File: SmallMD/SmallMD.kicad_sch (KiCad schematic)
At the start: 162 parts

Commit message: 回路設計
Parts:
- removed R? (x2): 1k, Resistor_SMD:R_0402_1005Metric, symbol Device:R
- removed R? (x2): 510, Resistor_SMD:R_0402_1005Metric, symbol Device:R
- removed U? (x2): TLP785, Package_DIP:DIP-4_W7.62mm, symbol Isolator:TLP785
- added C? (x4): 0.1uF, Capacitor_SMD:C_0402_1005Metric, symbol Device:C
- added JP? (x3): Jumper_2_Open, Connector_PinHeader_2.54mm:PinHeader_1x02_P2.54mm_Vertical, symbol Jumper:Jumper_2_Open
- added Q? (x3): 2PB709AR, Package_TO_SOT_SMD:SC-59_Handsoldering, symbol Device:Q_PNP_BEC
- added R? (x6): 2.2k, Resistor_SMD:R_0402_1005Metric, symbol Device:R
- added R? (x3): 20k, Resistor_SMD:R_0402_1005Metric, symbol Device:R
- added R? (x3): 120, Resistor_SMD:R_0402_1005Metric, symbol Device:R
- added R? (x2): 10k, Resistor_SMD:R_0402_1005Metric, symbol Device:R
- added R? (x3): 7.5k, Resistor_SMD:R_0603_1608Metric, symbol Device:R
- added R? (x2): 47, Resistor_SMD:R_0603_1608Metric, symbol Device:R
- added U? (x3): MAX3485, Package_SO:SOP-8_3.9x4.9mm_P1.27mm, symbol Interface_UART:MAX3485
- added U?: TLP2361, Package_SO:SO-6_4.4x3.6mm_P1.27mm, symbol Isolator:TLP2761
- R? (x2): value 510 -> 470
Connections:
- net +3.3V: now also C?.1, C?.1, C?.1, Q?.2 (E), Q?.2 (E), Q?.2 (E), R?.1, R?.1, R?.1, U?.8 (VCC), U?.8 (VCC), U?.8 (VCC)
- net +5V: now also C?.1, U?.6 (VDD), C?.1, U?.6 (VDD)
- net GND: now also C?.2, U?.3 (K), U?.4 (GND), C?.2, C?.2, C?.2, C?.2, R?.1, R?.1, R?.2, R?.2, R?.2, R?.2, R?.2, R?.2, U?.3 (K), U?.4 (GND), U?.5 (GND), U?.5 (GND), U?.5 (GND)
- net PWM_A: now also R?.1
- net PWM_B: now also R?.1
- net RS485_A: now also JP?.1 (A), JP?.1 (A), JP?.1 (A), R?.2, R?.2, R?.2, U?.6 (A), U?.6 (A), U?.6 (A)
- net RS485_B: now also R?.1, R?.1, R?.1, R?.2, R?.2, R?.2, U?.7 (B), U?.7 (B), U?.7 (B)
- net at Q?.1 (G), R?.2: now also R?.2 (x2)
- net at Q?.3 (D), R?.2: now also U?.1 (A) (x2)
- net at U?.2 (IN): now also R?.2, U?.5 (VO)
- net at U?.2 (IN): now also U?.5 (VO), R?.2
- new net: JP?.2 (B), R?.1 (x3)
- new net: Q?.3 (C), R?.1, U?.2 (~{RE}), U?.3 (DE) (x3)
- new net: R?.2, U?.4 (DI) (x3)
- new net: Q?.1 (B), R?.1 (x3)
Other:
- note added: "RS422"
- moved on the sheet: C?, D?, Q?, Q?A, Q?B, R?, U?

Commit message: 構成図追加
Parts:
- removed C? (x3): 0.1uF, Capacitor_SMD:C_0402_1005Metric, symbol Device:C
- removed D?: SBR1A40SA, Diode_SMD:D_SMA_Handsoldering, symbol Device:D_Schottky
- removed J?: Conn_01x10_Female, Connector_IDC:IDC-Header_2x05_P2.54mm_Horizontal, symbol Connector:Conn_01x10_Female
- removed JP? (x2): Jumper_2_Open, Connector_PinHeader_2.54mm:PinHeader_1x02_P2.54mm_Vertical, symbol Jumper:Jumper_2_Open
- removed Q? (x3): 2PB709AR, Package_TO_SOT_SMD:SC-59_Handsoldering, symbol Device:Q_PNP_BEC
- removed R? (x3): 20k, Resistor_SMD:R_0402_1005Metric, symbol Device:R
- removed R? (x2): 120, Resistor_SMD:R_0402_1005Metric, symbol Device:R
- removed R?: 39, Resistor_SMD:R_0603_1608Metric_Pad0.98x0.95mm_HandSolder, symbol Device:R
- removed R?: 10mR, symbol Device:R
- removed R? (x3): 7.5k, Resistor_SMD:R_0603_1608Metric, symbol Device:R
- removed R? (x4): 2.2k, Resistor_SMD:R_0402_1005Metric, symbol Device:R
- removed R?: 3.3k, Resistor_SMD:R_0603_1608Metric_Pad0.98x0.95mm_HandSolder, symbol Device:R
- removed U? (x2): MAX3485, Package_SO:SOP-8_3.9x4.9mm_P1.27mm, symbol Interface_UART:MAX3485
- removed U?: LT6106, Package_TO_SOT_SMD:SOT-23-5, symbol Amplifier_Current:LT6106
- added C20, C21, C?: 0.1uF, Capacitor_SMD:C_0402_1005Metric, symbol Device:C
- added D?: SBR1A40SA, Diode_SMD:D_SMA_Handsoldering, symbol Device:D_Schottky
- added J3: Conn_01x10_Male, BoxHeader_1.27mm:BoxHeader_2x05_P1.27mm_Vertical_SMD, symbol Connector:Conn_01x10_Male
- added J7: Conn_01x10_Male, Connector_IDC:IDC-Header_2x05_P2.54mm_Horizontal, symbol Connector:Conn_01x10_Male
- added J8: Conn_01x06_Male, symbol Connector:Conn_01x06_Male
- added JP1, JP2: Jumper_2_Open, Connector_PinHeader_2.54mm:PinHeader_1x02_P2.54mm_Vertical, symbol Jumper:Jumper_2_Open
- added R35, R36, R37, R38: 2.2k, Resistor_SMD:R_0402_1005Metric, symbol Device:R
- added R42, R43: 120, Resistor_SMD:R_0402_1005Metric, symbol Device:R
- added R?: 39, Resistor_SMD:R_0603_1608Metric_Pad0.98x0.95mm_HandSolder, symbol Device:R
- added R?: 10mR, symbol Device:R
- added R?: 3.3k, Resistor_SMD:R_0603_1608Metric_Pad0.98x0.95mm_HandSolder, symbol Device:R
- added U4, U5: MAX3485, Package_SO:SOP-8_3.9x4.9mm_P1.27mm, symbol Interface_UART:MAX3485
- added U?: LT6106, Package_TO_SOT_SMD:SOT-23-5, symbol Amplifier_Current:LT6106
- Q10, Q11, Q16, Q6, Q7: renamed from Q?; value 2PB709AR -> S8050; footprint Package_TO_SOT_SMD:SC-59_Handsoldering -> Package_TO_SOT_SMD:SOT-23
- Q14, Q15: renamed from Q?; footprint Package_TO_SOT_SMD:SOT-23_Handsoldering -> Package_TO_SOT_SMD:SOT-23
- Q18, Q19: renamed from Q?; footprint (none) -> Package_SO:SOP-8_3.9x4.9mm_P1.27mm
- SW3: renamed from SW?; footprint (none) -> Slide_Switch:SW_Slide_SPDT_White
- SW4: renamed from SW?; footprint Button_Switch_SMD:SW_SPST_Omron_B3FS-100xP -> Button_Switch_SMD:SW_Push_1P1T_NO_Vertical_Wuerth_434133025816
- U2: renamed from U?; value AZ1084CD-3.3 -> AZ1084CD-5.0
- Y1: renamed from Y?; footprint (none) -> Crystal:Crystal_SMD_HC49-SD_HandSoldering
- gave numbers to parts that had none: 148
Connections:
- net +3.3V: now also C20.1, C21.1, D?.1 (K), R35.1, R37.1, U4.8 (VCC), U5.8 (VCC)
- net +5V: now also J7.2 (Pin_2)
- net 3.3VBUS: now also J3.1 (Pin_1)
- net Current_Sence: now also D?.2 (A), R?.1, U?.1
- net GND: now also U12.2 (~{RE}), U12.3 (DE), U12.4 (DI), C20.2, C21.2, C?.1, J3.4 (Pin_4), J7.3 (Pin_3), J8.4 (Pin_4), R36.2, R38.2, R?.2, U4.2 (~{RE}), U4.3 (DE), U4.4 (DI), U4.5 (GND), U5.2 (~{RE}), U5.3 (DE), U5.4 (DI), U5.5 (GND), U?.2 (V-)
- net MainRX_STLinkTX: now also J3.8 (Pin_8)
- net MainTX_STLinkRX: now also J3.9 (Pin_9)
- net Motor_A: now also J8.2 (Pin_2)
- net Motor_B: now also J8.1 (Pin_1)
- net NRST: now also J3.6 (Pin_6)
- net RS485_A: no longer JP4.1 (A), R73.2, U12.6 (A)
- net RS485_B: no longer R74.1, R75.2, U12.7 (B)
- net TCK: now also J3.3 (Pin_3)
- net TMS: now also J3.5 (Pin_5)
- net VCC: now also C25.1, C26.1, D15.2 (A), D16.2 (A), U10.1 (VCC), U11.1 (VCC), C?.2, U?.5 (V+)
- net VDD: now also R?.2, R?.2
- net Vdrive: now also R?.1, U?.4 (+); no longer C25.1, C26.1, D15.2 (A), D16.2 (A), U10.1 (VCC), U11.1 (VCC)
- net Encoder_I: now reaches U12.1 (RO)
- net Encoder_I: now also JP4.1 (A), R73.2, U12.6 (A), J7.10 (Pin_10)
- new net: JP1.2 (B), R42.1
- new net: R?.1, U?.3 (-)
- new net: JP2.2 (B), R43.1
- new net Encoder_A: J7.6 (Pin_6), J8.5 (Pin_5), JP1.1 (A), R35.2, U4.1 (RO), U4.6 (A)
- new net Encoder_B: J7.8 (Pin_8), J8.6 (Pin_6), JP2.1 (A), R37.2, U5.1 (RO), U5.6 (A)
- new net Encoder_invA: J7.5 (Pin_5), R36.1, R42.2, U4.7 (B)
- new net Encoder_invB: J7.7 (Pin_7), R38.1, R43.2, U5.7 (B)
- new net Encoder_invI: J7.9 (Pin_9), R74.1, R75.2, U12.7 (B)
- no-connect marks 19 -> 7
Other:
- note added: "Conn to Encoder"
- moved on the sheet: C30, JP4, R73, R74, R75, U12

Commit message: diagram_SmallPW
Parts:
- C1, C7: value 4.7uF -> 1uF; footprint Capacitor_SMD:C_0603_1608Metric -> Capacitor_SMD:C_0402_1005Metric
- gave numbers to parts that had none: 6

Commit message: 回路図pdf出力
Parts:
- added R46, R52, R53: 40mR, Resistor_SMD:R_2512_6332Metric, symbol Device:R
- R39: value 10mR -> 40mR; footprint (none) -> Resistor_SMD:R_2512_6332Metric
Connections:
- net VDD: now also R46.2, R52.2, R53.2
- net Vdrive: now also R46.1, R52.1, R53.1
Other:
- moved on the sheet: C19, D14, R44, R45, U6

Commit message: 進捗
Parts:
- removed C15, C16: 470uF, Capacitor_SMD:C_Elec_8x10.2, symbol Device:C_Polarized
- removed C8: ADJ_ST, Capacitor_SMD:C_0603_1608Metric, symbol Device:C
- removed D11, D12: Green, LED_SMD:LED_0603_1608Metric_Pad1.05x0.95mm_HandSolder, symbol Device:LED
- removed D9: D_Zener, Diode_SMD:D_SOD-323_HandSoldering, symbol Device:D_Zener
- removed H1, H3: MountingHole_Pad, TestPoint:TestPoint_Pad_1.5x1.5mm, symbol Mechanical:MountingHole_Pad
- removed H4, H6, H8: MountingHole, MountingHole:MountingHole_3.2mm_M3, symbol Mechanical:MountingHole
- removed Q10, Q11, Q6, Q7: S8050, Package_TO_SOT_SMD:SOT-23, symbol Device:Q_PNP_BEC
- removed Q4, Q5, Q8, Q9: SSM3J332R, Package_TO_SOT_SMD:SOT-23W, symbol Device:Q_PMOS_GSD
- removed R20, R21, R24, R25, R26, R27, R28, R29, R30: 10k, Resistor_SMD:R_0402_1005Metric, symbol Device:R
- removed R22, R32, R33: 1k, Resistor_SMD:R_0402_1005Metric, symbol Device:R
- removed R23: 100k, Resistor_SMD:R_0402_1005Metric, symbol Device:R
- added JP5, JP6: SolderJumper_3_Bridged12, Jumper:SolderJumper-3_P2.0mm_Open_TrianglePad1.0x1.5mm_NumberLabels, symbol Jumper:SolderJumper_3_Bridged12
- C17, C18: value 4.7uF -> 10uF; footprint Capacitor_SMD:C_0805_2012Metric_Pad1.18x1.45mm_HandSolder -> Capacitor_SMD:C_0805_2012Metric
- C2: value 0.1uF -> 10uF; footprint Capacitor_SMD:C_0402_1005Metric -> Capacitor_SMD:C_0805_2012Metric
- C7: value 1uF -> 10uF; footprint Capacitor_SMD:C_0402_1005Metric -> Capacitor_SMD:C_0805_2012Metric
- D1, D14, D7, D8: value SBR1A40SA -> 1N5819WS; footprint Diode_SMD:D_SMA_Handsoldering -> Diode_SMD:D_SOD-323_HandSoldering
- D15, D16: value SBR1A40SA -> SS2040FL; footprint Diode_SMD:D_SMA_Handsoldering -> Diode_SMD:D_SOD-123
- J1: footprint Connector_AMASS:AMASS_XT30PW-M_1x02_P2.50mm_Horizontal -> Connector_AMASS:AMASS_XT30U-M_1x02_P5.0mm_Vertical
- J2, J4: footprint Connector_AMASS:AMASS_XT30PW-F_1x02_P2.50mm_Horizontal -> Connector_AMASS:AMASS_XT30U-F_1x02_P5.0mm_Vertical
- J5, J6: footprint Connector_Molex:Molex_SPOX_5268-04A_1x04_P2.50mm_Horizontal -> Connector_Molex:Molex_SPOX_5267-04A_1x04_P2.50mm_Vertical
- J7: footprint Connector_IDC:IDC-Header_2x05_P2.54mm_Horizontal -> Connector_IDC:IDC-Header_2x05_P2.54mm_Vertical
- J8: footprint (none) -> Connector_JST:JST_PH_B6B-PH-K_1x06_P2.00mm_Vertical
- Y1: footprint Crystal:Crystal_SMD_HC49-SD_HandSoldering -> Crystal:Crystal_SMD_HC49-SD
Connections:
- net 3.3VSYS is gone; now on net +3.3V: C5.1, C7.1, D7.2 (A), R18.2, U1.2 (VO)
- net +5V: now also C2.1, J8.3 (Pin_3)
- net Encoder_A: now also JP5.2 (C); no longer J7.6 (Pin_6), J8.5 (Pin_5), JP1.1 (A), R35.2, U4.1 (RO), U4.6 (A)
- net Encoder_B: now also JP6.2 (C); no longer J7.8 (Pin_8), J8.6 (Pin_6), JP2.1 (A), R37.2, U5.1 (RO), U5.6 (A)
- net GND: now also C7.2
- net 12VBAT renamed 7.4VBAT
- net 3.3VBUS: no longer names the net of J3.1 (Pin_1)
- net 3.3VBUS: no longer C2.1
- net Encoder_I renamed Maxon_RS422_I
- net Maxon_RS422_I: no longer U12.1 (RO)
- net Encoder_invA renamed Maxon_RS422_invA
- net Encoder_invB renamed Maxon_RS422_invB
- net Encoder_invI renamed Maxon_RS422_invI
- new net Akitsuki_A: J8.5 (Pin_5), JP5.3 (B)
- new net Akitsuki_B: J8.6 (Pin_6), JP6.3 (B)
- new net Maxon_A: JP5.1 (A), U4.1 (RO)
- new net Maxon_B: JP6.1 (A), U5.1 (RO)
- new net Maxon_I: U12.1 (RO)
- new net Maxon_RS422_A: J7.6 (Pin_6), JP1.1 (A), R35.2, U4.6 (A)
- new net Maxon_RS422_B: J7.8 (Pin_8), JP2.1 (A), R37.2, U5.6 (A)
- no-connect marks 7 -> 8
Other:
- note added: "Switch Encoder OUT"
- note removed: "理想ダイオード/3.3VSYS"
- note removed: "電源切替/STLink"
- moved on the sheet: C13, C14, C20, C21, C24, C30, D10, D13, J5, J6, J8, JP1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

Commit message: エンコーダー基板配線完了
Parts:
- removed C10, C9: 22pF, Capacitor_SMD:C_0603_1608Metric, symbol Device:C
- removed R52, R53: 40mR, Resistor_SMD:R_2512_6332Metric, symbol Device:R
- removed Y1: 48MHz, Crystal:Crystal_SMD_HC49-SD, symbol Device:Crystal
- added C8: 0.1uF, Capacitor_SMD:C_0402_1005Metric, symbol Device:C
- added U13: NJU6319AE, Package_SO:SOP-8_3.9x4.9mm_P1.27mm, symbol CrystalOSC_Control:NJU6319AE
- added Y1: 16MHz, Crystal:Crystal_SMD_3225-4Pin_3.2x2.5mm_HandSoldering, symbol Device:Crystal_GND24
- R39, R46: value 40mR -> 20mR
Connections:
- net +3.3V: now also C8.1, U13.1 (~{CONT}), U13.8 (VDD)
- net GND: now also C8.2, U13.4 (VSS), Y1.2, Y1.4
- net NRST: now also U3.6 (PF2-NRST)
- net OSC_IN: now also U3.2 (PC14-OSCX_IN), U13.5 (FOUT)
- new net: U13.2 (XT), Y1.1
- new net: U13.3 (~{XT}), Y1.3
- new net: U13.6 (NC), U13.7 (NC)
- no-connect marks 8 -> 9
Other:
- moved on the sheet: C11, C12, C19, D14, H2, R44, R45, R46, SW4, U6

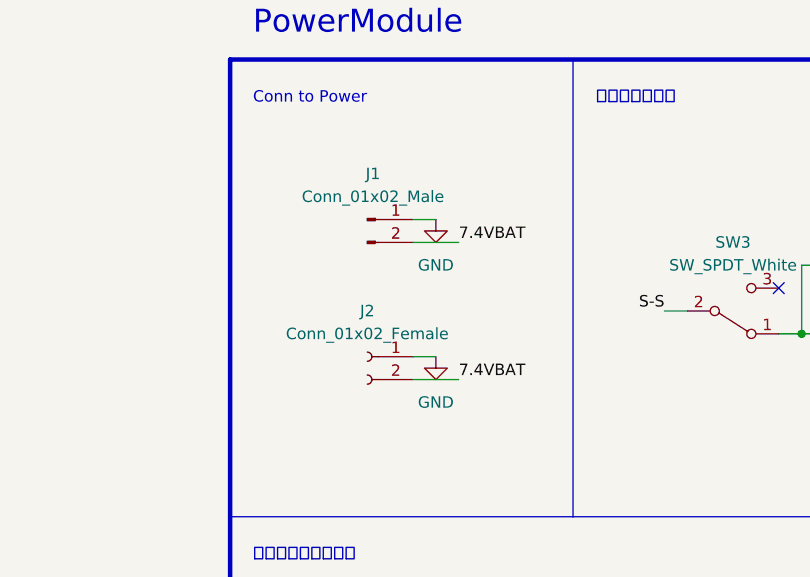
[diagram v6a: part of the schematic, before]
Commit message: 人力曲面配線中
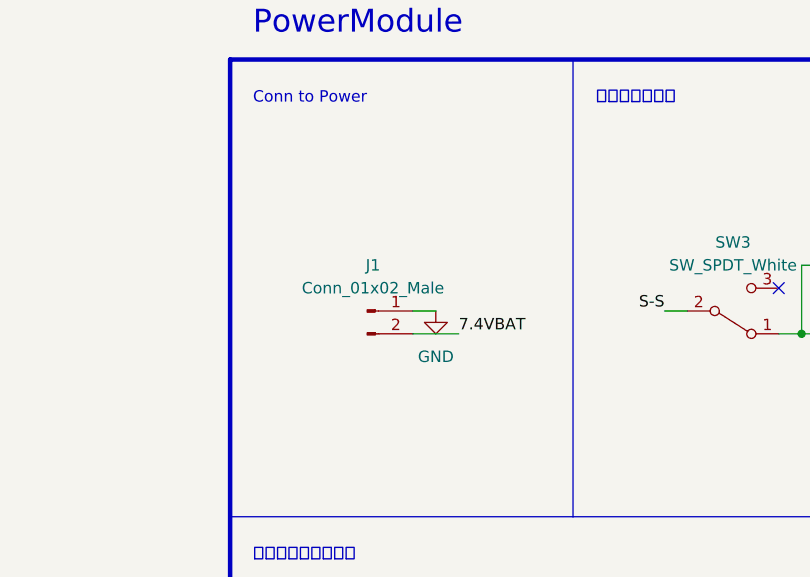
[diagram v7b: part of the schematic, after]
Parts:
- removed J2: Conn_01x02_Female, Connector_AMASS:AMASS_XT30U-F_1x02_P5.0mm_Vertical, symbol Connector:Conn_01x02_Female
- JP1, JP2, JP4: footprint Connector_PinHeader_2.54mm:PinHeader_1x02_P2.54mm_Vertical -> Jumper:SolderJumper-2_P1.3mm_Open_TrianglePad1.0x1.5mm
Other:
- moved on the sheet: J1
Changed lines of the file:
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@@
     (stroke (width 0) (type default) (color 0 0 0 0))
   )
-  (wire (pts (xy 127 106.68) (xy 132.08 106.68))
+  (wire (pts (xy 127 116.84) (xy 132.08 116.84))
     (stroke (width 0) (type default) (color 0 0 0 0))
   )
@@
     (stroke (width 0) (type default) (color 0 0 0 0))
   )
-  (wire (pts (xy 127 121.92) (xy 132.08 121.92))
-    (stroke (width 0) (type default) (color 0 0 0 0))
-  )
   (wire (pts (xy 233.68 199.39) (xy 233.68 203.2))
     (stroke (width 0) (type default) (color 0 0 0 0))
@@
     (stroke (width 0) (type default) (color 0 0 0 0))
   )
-  (wire (pts (xy 127 119.38) (xy 129.54 119.38))
-    (stroke (width 0) (type default) (color 0 0 0 0))
-  )
   (wire (pts (xy 314.96 167.64) (xy 314.96 168.91))
     (stroke (width 0) (type default) (color 0 0 0 0))
@@
     (stroke (width 0) (type default) (color 0 0 0 0))
   )
-  (wire (pts (xy 127 104.14) (xy 129.54 104.14))
+  (wire (pts (xy 127 114.3) (xy 129.54 114.3))
     (stroke (width 0) (type default) (color 0 0 0 0))
   )
@@
     (effects (font (size 1.27 1.27)) (justify right bottom))
   )
-  (label "7.4VBAT" (at 132.08 106.68 0)
+  (label "7.4VBAT" (at 132.08 116.84 0)
     (effects (font (size 1.27 1.27)) (justify left bottom))
   )
@@
     (effects (font (size 1.27 1.27)) (justify right bottom))
   )
-  (label "7.4VBAT" (at 132.08 121.92 0)
-    (effects (font (size 1.27 1.27)) (justify left bottom))
-  )
   (label "S-S" (at 139.7 165.1 0)
     (effects (font (size 1.27 1.27)) (justify left bottom))
@@
     (property "Reference" "JP2" (id 0) (at 673.1 162.56 0))
     (property "Value" "Jumper_2_Open" (id 1) (at 673.1 165.1 0))
-    (property "Footprint" "Connector_PinHeader_2.54mm:PinHeader_1x02_P2.54mm_Vertical" (id 2) (at 678.18 160.02 0)
+    (property "Footprint" "Jumper:SolderJumper-2_P1.3mm_Open_TrianglePad1.0x1.5mm" (id 2) (at 678.18 160.02 0)
       (effects (font (size 1.27 1.27)) hide)
     )
@@
     (pin "9")
   )
-  (symbol (lib_id "Connector:Conn_01x02_Male") (at 121.92 104.14 0) (unit 1)
+  (symbol (lib_id "Connector:Conn_01x02_Male") (at 121.92 114.3 0) (unit 1)
     (in_bom yes) (on_board yes) (fields_autoplaced)
-    (property "Reference" "J1" (id 0) (at 122.555 99.06 0))
-    (property "Value" "Conn_01x02_Male" (id 1) (at 122.555 101.6 0))
-    (property "Footprint" "Connector_AMASS:AMASS_XT30U-M_1x02_P5.0mm_Vertical" (id 2) (at 121.92 104.14 0)
+    (property "Reference" "J1" (id 0) (at 122.555 109.22 0))
+    (property "Value" "Conn_01x02_Male" (id 1) (at 122.555 111.76 0))
+    (property "Footprint" "Connector_AMASS:AMASS_XT30U-M_1x02_P5.0mm_Vertical" (id 2) (at 121.92 114.3 0)
       (effects (font (size 1.27 1.27)) hide)
     )
-    (property "Datasheet" "~" (id 3) (at 121.92 104.14 0)
+    (property "Datasheet" "~" (id 3) (at 121.92 114.3 0)
       (effects (font (size 1.27 1.27)) hide)
     )
@@
     (property "Reference" "JP4" (id 0) (at 635 200.66 0))
     (property "Value" "Jumper_2_Open" (id 1) (at 635 203.2 0))
-    (property "Footprint" "Connector_PinHeader_2.54mm:PinHeader_1x02_P2.54mm_Vertical" (id 2) (at 640.08 198.12 0)
+    (property "Footprint" "Jumper:SolderJumper-2_P1.3mm_Open_TrianglePad1.0x1.5mm" (id 2) (at 640.08 198.12 0)
       (effects (font (size 1.27 1.27)) hide)
     )
@@
     (pin "2")
   )
-  (symbol (lib_id "Connector:Conn_01x02_Female") (at 121.92 119.38 0) (mirror y) (unit 1)
-    (in_bom yes) (on_board yes)
-    (property "Reference" "J2" (id 0) (at 121.92 114.3 0))
-    (property "Value" "Conn_01x02_Female" (id 1) (at 121.92 116.84 0))
-    (property "Footprint" "Connector_AMASS:AMASS_XT30U-F_1x02_P5.0mm_Vertical" (id 2) (at 121.92 119.38 0)
-      (effects (font (size 1.27 1.27)) hide)
-    )
-    (property "Datasheet" "~" (id 3) (at 121.92 119.38 0)
-      (effects (font (size 1.27 1.27)) hide)
-    )
-    (pin "1")
-    (pin "2")
-  )
   (symbol (lib_id "Device:R") (at 617.22 480.06 180) (unit 1)
     (in_bom yes) (on_board yes)
@@
     (pin "1")
   )
-  (symbol (lib_id "power:GND") (at 129.54 119.38 0) (unit 1)
-    (in_bom yes) (on_board yes) (fields_autoplaced)
-    (property "Reference" "#PWR06" (id 0) (at 129.54 125.73 0)
-      (effects (font (size 1.27 1.27)) hide)
-    )
-    (property "Value" "GND" (id 1) (at 129.54 124.46 0))
-    (property "Footprint" "" (id 2) (at 129.54 119.38 0)
-      (effects (font (size 1.27 1.27)) hide)
-    )
-    (property "Datasheet" "" (id 3) (at 129.54 119.38 0)
-      (effects (font (size 1.27 1.27)) hide)
-    )
-    (pin "1")
-  )
   (symbol (lib_id "Device:LED") (at 713.74 353.06 270) (unit 1)
     (in_bom yes) (on_board yes)
@@
     (pin "2")
   )
-  (symbol (lib_id "power:GND") (at 129.54 104.14 0) (unit 1)
+  (symbol (lib_id "power:GND") (at 129.54 114.3 0) (unit 1)
     (in_bom yes) (on_board yes) (fields_autoplaced)
-    (property "Reference" "#PWR05" (id 0) (at 129.54 110.49 0)
+    (property "Reference" "#PWR05" (id 0) (at 129.54 120.65 0)
       (effects (font (size 1.27 1.27)) hide)
     )
-    (property "Value" "GND" (id 1) (at 129.54 109.22 0))
-    (property "Footprint" "" (id 2) (at 129.54 104.14 0)
+    (property "Value" "GND" (id 1) (at 129.54 119.38 0))
+    (property "Footprint" "" (id 2) (at 129.54 114.3 0)
       (effects (font (size 1.27 1.27)) hide)
     )
-    (property "Datasheet" "" (id 3) (at 129.54 104.14 0)
+    (property "Datasheet" "" (id 3) (at 129.54 114.3 0)
       (effects (font (size 1.27 1.27)) hide)
     )
@@
     (property "Reference" "JP1" (id 0) (at 635 124.46 0))
     (property "Value" "Jumper_2_Open" (id 1) (at 635 127 0))
-    (property "Footprint" "Connector_PinHeader_2.54mm:PinHeader_1x02_P2.54mm_Vertical" (id 2) (at 640.08 121.92 0)
+    (property "Footprint" "Jumper:SolderJumper-2_P1.3mm_Open_TrianglePad1.0x1.5mm" (id 2) (at 640.08 121.92 0)
       (effects (font (size 1.27 1.27)) hide)
     )
@@
       (reference "#PWR05") (unit 1) (value "GND") (footprint "")
     )
-    (path "/911b2580-97c4-4cab-9cac-51890a1bea7f"
-      (reference "#PWR06") (unit 1) (value "GND") (footprint "")
-    )
     (path "/de171a8e-a785-4f50-9c76-3eaf1d3986b9"
       (reference "#PWR07") (unit 1) (value "GND") (footprint "")
@@
       (reference "J1") (unit 1) (value "Conn_01x02_Male") (footprint "Connector_AMASS:AMASS_XT30U-M_1x02_P5.0mm_Vertical")
     )
-    (path "/86c59a3f-7256-4c56-8937-2b12f48c99a3"
-      (reference "J2") (unit 1) (value "Conn_01x02_Female") (footprint "Connector_AMASS:AMASS_XT30U-F_1x02_P5.0mm_Vertical")
-    )
     (path "/2b8c4489-5650-41e0-ae54-1b2436e25a1e"
       (reference "J3") (unit 1) (value "Conn_01x10_Male") (footprint "BoxHeader_1.27mm:BoxHeader_2x05_P1.27mm_Vertical_SMD")
@@
     )
     (path "/d61a2c7c-0262-4a59-bda7-d2a472021b68"
-      (reference "JP1") (unit 1) (value "Jumper_2_Open") (footprint "Connector_PinHeader_2.54mm:PinHeader_1x02_P2.54mm_Vertical")
+      (reference "JP1") (unit 1) (value "Jumper_2_Open") (footprint "Jumper:SolderJumper-2_P1.3mm_Open_TrianglePad1.0x1.5mm")
     )
     (path "/0d475095-2e46-495b-87ae-d5a9f2c224d6"
-      (reference "JP2") (unit 1) (value "Jumper_2_Open") (footprint "Connector_PinHeader_2.54mm:PinHeader_1x02_P2.54mm_Vertical")
+      (reference "JP2") (unit 1) (value "Jumper_2_Open") (footprint "Jumper:SolderJumper-2_P1.3mm_Open_TrianglePad1.0x1.5mm")
     )
     (path "/d8619807-4c54-4296-9272-4fb316bd1701"
@@
     )
     (path "/84edd06f-f298-4489-8f56-6d4999bc4671"
-      (reference "JP4") (unit 1) (value "Jumper_2_Open") (footprint "Connector_PinHeader_2.54mm:PinHeader_1x02_P2.54mm_Vertical")
+      (reference "JP4") (unit 1) (value "Jumper_2_Open") (footprint "Jumper:SolderJumper-2_P1.3mm_Open_TrianglePad1.0x1.5mm")
     )
     (path "/bac6db02-12d9-4f03-ac80-5c5c1207db88"

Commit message: LargeMDほぼ完成
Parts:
- U3: value STM32C031K4T6 -> STM32G030K6T6
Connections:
- net MainRX_RS485TX is gone; now on net MainRX2_RS485TX: U7.1 (RO)
- net MainRX_STLinkTX is gone; now on net MainRX1_STLinkTX: J3.8 (Pin_8)
- net MainTX_RS485RX is gone; now on net MainTX2_RS485RX: R49.2, U7.4 (DI)
- net MainTX_STLinkRX is gone; now on net MainTX1_STLinkRX: J3.9 (Pin_9)
- net Encoder_A: now also U3.14 (PA7)
- net Encoder_B: now also U3.20 (PC6)
- net PWM_A: now also U3.13 (PA6)
- net TCK: now also U3.25 (PA14-BOOT0)
- net TMS: now also U3.24 (PA13)
- net MainTX1_STLinkRX: now reaches U3.19 (PA9)
- net MainRX1_STLinkTX: now reaches U3.21 (PA10)
- net MainRX2_RS485TX: now reaches U3.26 (PA15)
- net MainTX2_RS485RX: now reaches U3.9 (PA2)
- net at U13.6 (NC): no longer U13.7 (NC)
